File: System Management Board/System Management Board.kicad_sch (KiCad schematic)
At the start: 21 parts

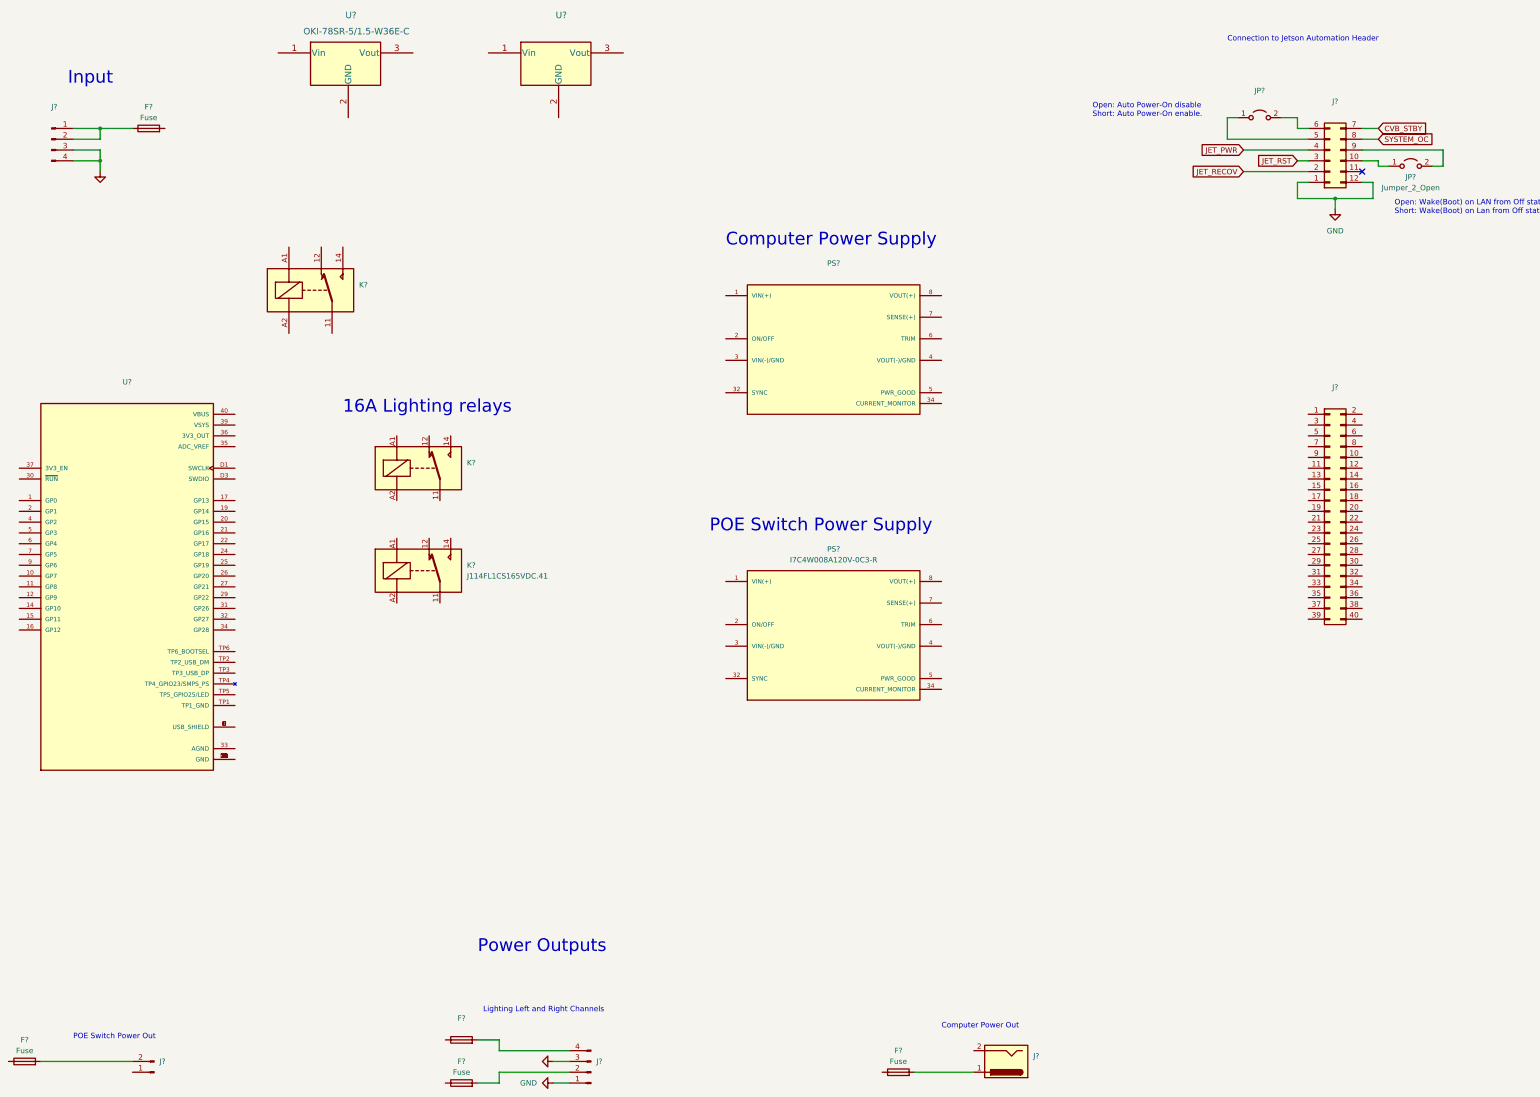
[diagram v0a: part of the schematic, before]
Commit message: Started playing around with layout and mounting of SMB in Enclosure
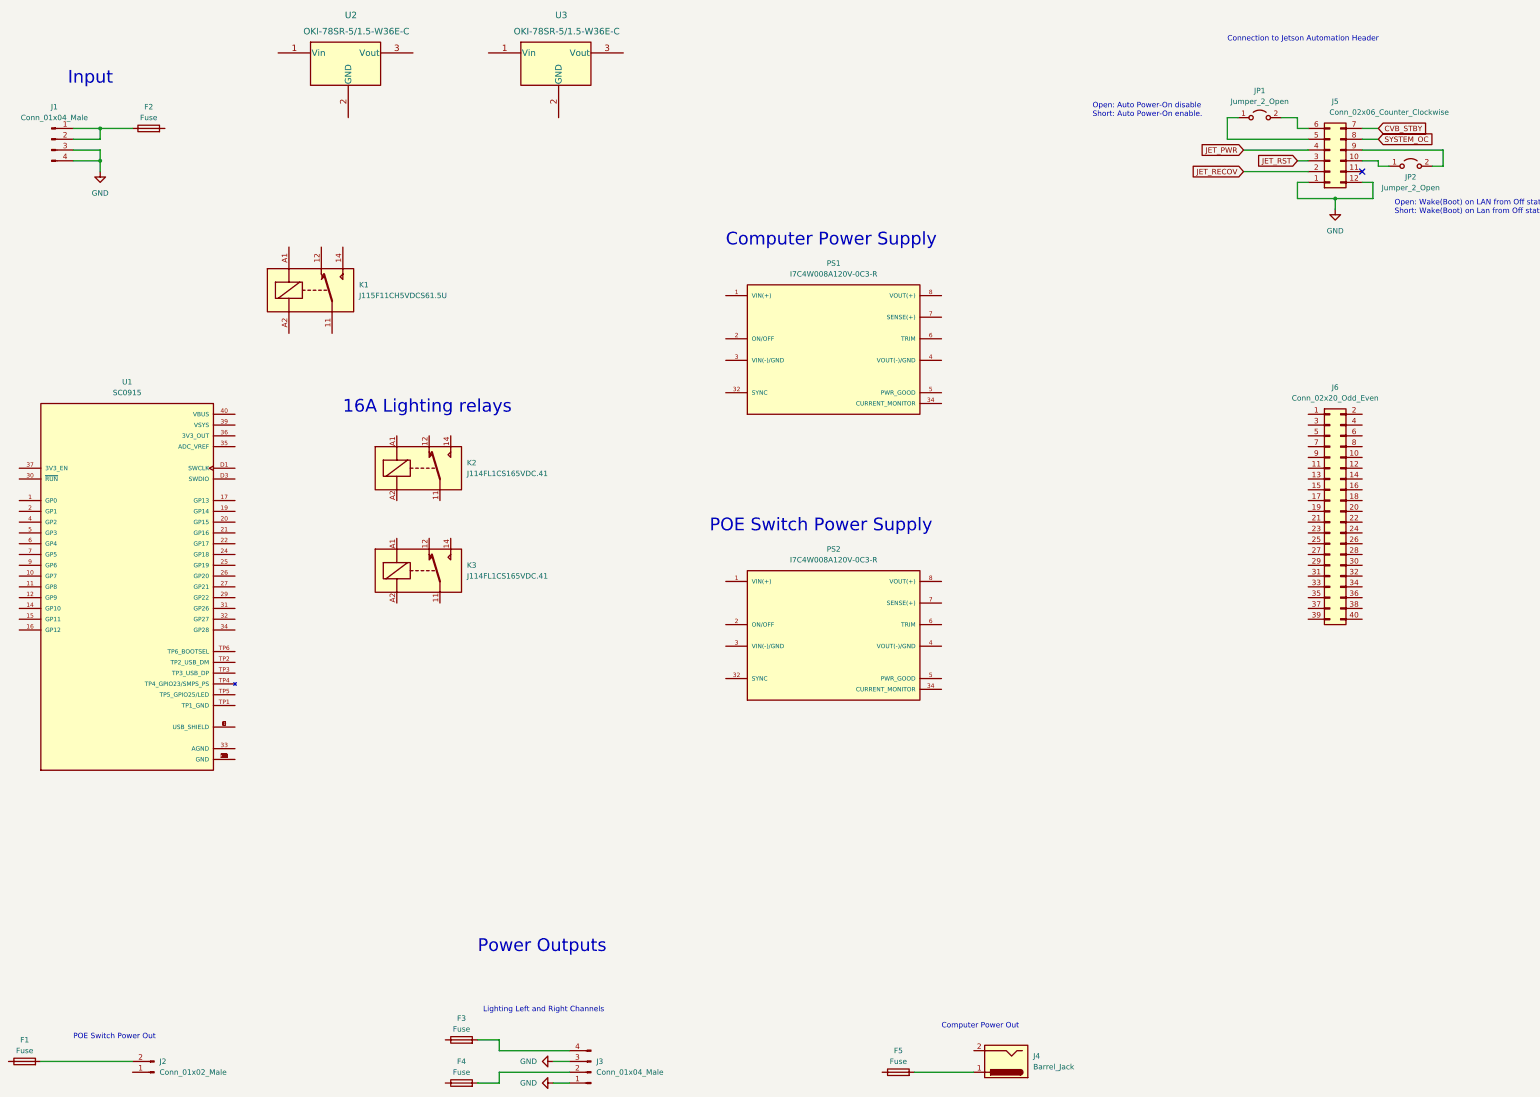
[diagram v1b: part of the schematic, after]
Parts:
- F3: renamed from F?; value (none) -> Fuse
- J1, J3: renamed from J?; value (none) -> Conn_01x04_Male
- J2: renamed from J?; value (none) -> Conn_01x02_Male
- J4: renamed from J?; value (none) -> Barrel_Jack
- J5: renamed from J?; value (none) -> Conn_02x06_Counter_Clockwise
- J6: renamed from J?; value (none) -> Conn_02x20_Odd_Even; footprint (none) -> Connector_PinSocket_2.54mm:PinSocket_2x20_P2.54mm_Horizontal
- JP1: renamed from JP?; value (none) -> Jumper_2_Open
- K1: renamed from K?; value (none) -> J115F11CH5VDCS61.5U; footprint (none) -> SMB:Relay_SPDT_RAYEX-L90S
- K2: renamed from K?; value (none) -> J114FL1CS165VDC.41; footprint (none) -> SMB:Relay_SPDT_Schrack-RT1-16A-FormC_RM5mm
- PS1: renamed from PS?; value (none) -> I7C4W008A120V-0C3-R; footprint (none) -> SMB:CONV_I7C4W008A120V-0C3-R
- PS2: renamed from PS?; footprint CONV_I7C4W008A120V-0C3-R -> SMB:CONV_I7C4W008A120V-0C3-R
- U1: renamed from U?; value (none) -> SC0915; footprint (none) -> SMB:MODULE_SC0915
- U3: renamed from U?; value (none) -> OKI-78SR-5/1.5-W36E-C
- gave numbers to parts that had none: 7

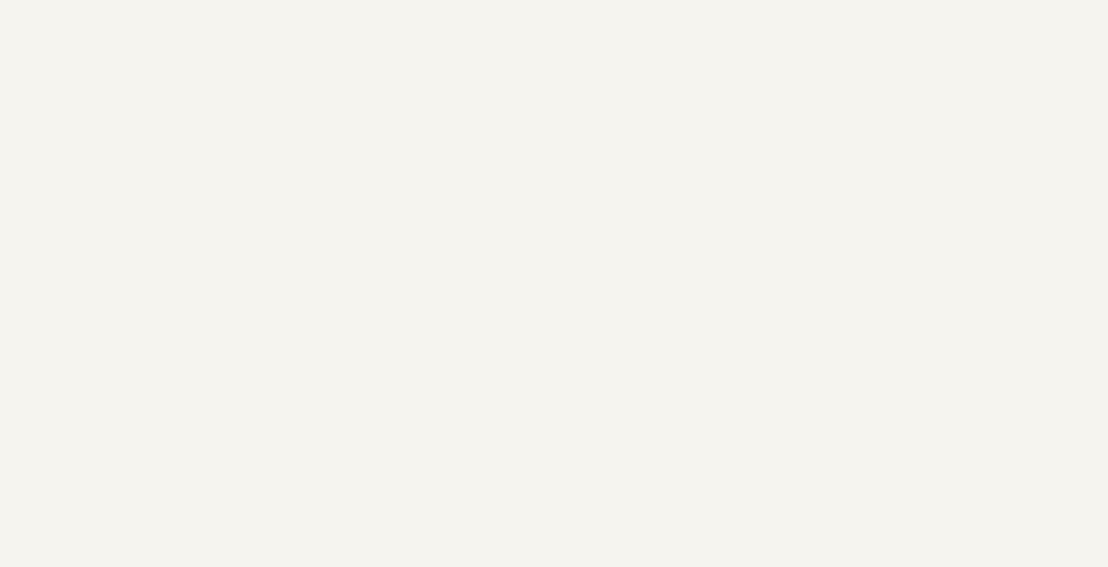
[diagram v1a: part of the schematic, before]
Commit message: Fixed solidworks brainmelt from last commit and moved PCb template into Kicad
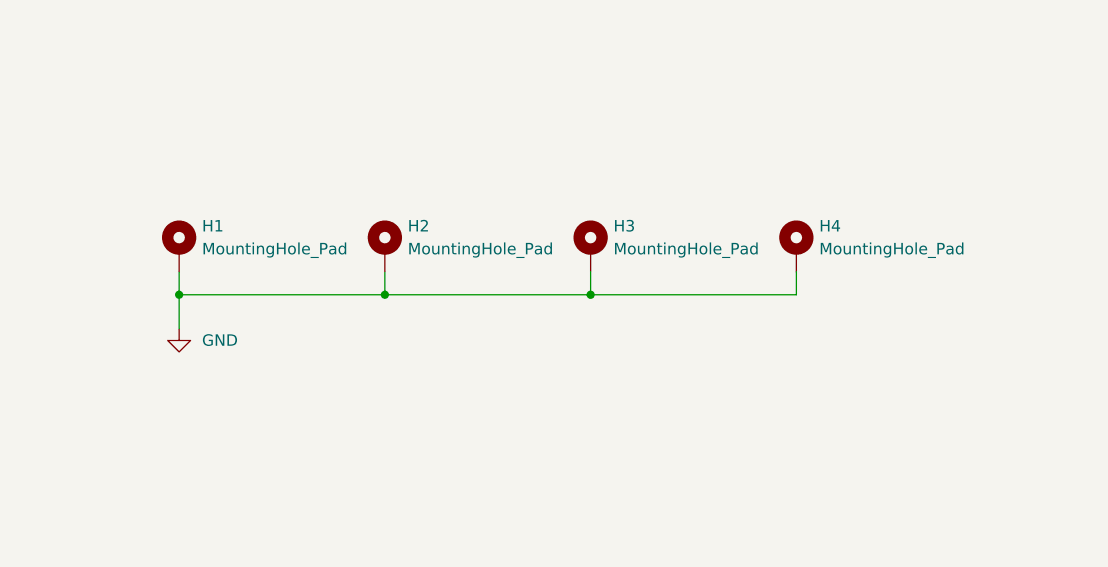
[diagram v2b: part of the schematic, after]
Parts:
- added H1, H2, H3, H4: MountingHole_Pad, MountingHole:MountingHole_3.2mm_M3_DIN965_Pad, symbol Mechanical:MountingHole_Pad
- J6: footprint Connector_PinSocket_2.54mm:PinSocket_2x20_P2.54mm_Horizontal -> Connector_PinHeader_2.54mm:PinHeader_2x20_P2.54mm_Horizontal
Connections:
- net GND: now also H1.1, H2.1, H3.1, H4.1
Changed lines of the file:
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@@
   (junction (at 48.26 45.72) (diameter 0) (color 0 0 0 0)
+  )
+  (junction (at 359.41 240.03) (diameter 0) (color 0 0 0 0)
+  )
+  (junction (at 336.55 240.03) (diameter 0) (color 0 0 0 0)
+  )
+  (junction (at 313.69 240.03) (diameter 0) (color 0 0 0 0)
   )
   (junction (at 339.09 62.23) (diameter 0) (color 0 0 0 0)
@@
     (stroke (width 0) (type default) (color 0 0 0 0))
   )
+  (wire (pts (xy 336.55 240.03) (xy 359.41 240.03))
+    (stroke (width 0) (type default) (color 0 0 0 0))
+  )
+  (wire (pts (xy 359.41 240.03) (xy 382.27 240.03))
+    (stroke (width 0) (type default) (color 0 0 0 0))
+  )
+  (wire (pts (xy 382.27 237.49) (xy 382.27 240.03))
+    (stroke (width 0) (type default) (color 0 0 0 0))
+  )
   (wire (pts (xy 351.79 54.61) (xy 349.25 54.61))
     (stroke (width 0) (type default) (color 0 0 0 0))
@@
     (stroke (width 0) (type default) (color 0 0 0 0))
   )
+  (wire (pts (xy 313.69 240.03) (xy 313.69 243.84))
+    (stroke (width 0) (type default) (color 0 0 0 0))
+  )
   (wire (pts (xy 317.5 50.8) (xy 332.74 50.8))
     (stroke (width 0) (type default) (color 0 0 0 0))
@@
     (stroke (width 0) (type default) (color 0 0 0 0))
   )
+  (wire (pts (xy 359.41 237.49) (xy 359.41 240.03))
+    (stroke (width 0) (type default) (color 0 0 0 0))
+  )
+  (wire (pts (xy 313.69 240.03) (xy 336.55 240.03))
+    (stroke (width 0) (type default) (color 0 0 0 0))
+  )
   (wire (pts (xy 364.49 50.8) (xy 364.49 54.61))
     (stroke (width 0) (type default) (color 0 0 0 0))
@@
     (stroke (width 0) (type default) (color 0 0 0 0))
   )
+  (wire (pts (xy 313.69 237.49) (xy 313.69 240.03))
+    (stroke (width 0) (type default) (color 0 0 0 0))
+  )
   (wire (pts (xy 330.2 62.23) (xy 339.09 62.23))
+    (stroke (width 0) (type default) (color 0 0 0 0))
+  )
+  (wire (pts (xy 336.55 237.49) (xy 336.55 240.03))
     (stroke (width 0) (type default) (color 0 0 0 0))
   )
@@
     (pin "2")
   )
+  (symbol (lib_id "Mechanical:MountingHole_Pad") (at 313.69 234.95 0) (unit 1)
+    (in_bom yes) (on_board yes) (fields_autoplaced)
+    (property "Reference" "H1" (id 0) (at 316.23 232.4099 0)
+      (effects (font (size 1.27 1.27)) (justify left))
+    )
+    (property "Value" "MountingHole_Pad" (id 1) (at 316.23 234.9499 0)
+      (effects (font (size 1.27 1.27)) (justify left))
+    )
+    (property "Footprint" "MountingHole:MountingHole_3.2mm_M3_DIN965_Pad" (id 2) (at 313.69 234.95 0)
+      (effects (font (size 1.27 1.27)) hide)
+    )
+    (property "Datasheet" "~" (id 3) (at 313.69 234.95 0)
+      (effects (font (size 1.27 1.27)) hide)
+    )
+    (pin "1")
+  )
   (symbol (lib_id "Jumper:Jumper_2_Open") (at 356.87 54.61 0) (unit 1)
     (in_bom yes) (on_board yes)
@@
     (pin "1")
     (pin "2")
+  )
+  (symbol (lib_id "Mechanical:MountingHole_Pad") (at 382.27 234.95 0) (unit 1)
+    (in_bom yes) (on_board yes) (fields_autoplaced)
+    (property "Reference" "H4" (id 0) (at 384.81 232.4099 0)
+      (effects (font (size 1.27 1.27)) (justify left))
+    )
+    (property "Value" "MountingHole_Pad" (id 1) (at 384.81 234.9499 0)
+      (effects (font (size 1.27 1.27)) (justify left))
+    )
+    (property "Footprint" "MountingHole:MountingHole_3.2mm_M3_DIN965_Pad" (id 2) (at 382.27 234.95 0)
+      (effects (font (size 1.27 1.27)) hide)
+    )
+    (property "Datasheet" "~" (id 3) (at 382.27 234.95 0)
+      (effects (font (size 1.27 1.27)) hide)
+    )
+    (pin "1")
   )
   (symbol (lib_id "Device:Fuse") (at 133.35 270.51 90) (unit 1)
@@
     (property "Reference" "J6" (id 0) (at 339.09 106.68 0))
     (property "Value" "Conn_02x20_Odd_Even" (id 1) (at 339.09 109.22 0))
-    (property "Footprint" "Connector_PinSocket_2.54mm:PinSocket_2x20_P2.54mm_Horizontal" (id 2) (at 337.82 135.89 0)
+    (property "Footprint" "Connector_PinHeader_2.54mm:PinHeader_2x20_P2.54mm_Horizontal" (id 2) (at 337.82 135.89 0)
       (effects (font (size 1.27 1.27)) hide)
     )
@@
     (pin "9")
   )
+  (symbol (lib_id "power:GND") (at 313.69 243.84 0) (unit 1)
+    (in_bom yes) (on_board yes) (fields_autoplaced)
+    (property "Reference" "#PWR0105" (id 0) (at 313.69 250.19 0)
+      (effects (font (size 1.27 1.27)) hide)
+    )
+    (property "Value" "GND" (id 1) (at 316.23 245.1099 0)
+      (effects (font (size 1.27 1.27)) (justify left))
+    )
+    (property "Footprint" "" (id 2) (at 313.69 243.84 0)
+      (effects (font (size 1.27 1.27)) hide)
+    )
+    (property "Datasheet" "" (id 3) (at 313.69 243.84 0)
+      (effects (font (size 1.27 1.27)) hide)
+    )
+    (pin "1")
+  )
   (symbol (lib_id "Device:Fuse") (at 59.69 45.72 90) (unit 1)
     (in_bom yes) (on_board yes)
@@
     (pin "1")
   )
+  (symbol (lib_id "Mechanical:MountingHole_Pad") (at 336.55 234.95 0) (unit 1)
+    (in_bom yes) (on_board yes) (fields_autoplaced)
+    (property "Reference" "H2" (id 0) (at 339.09 232.4099 0)
+      (effects (font (size 1.27 1.27)) (justify left))
+    )
+    (property "Value" "MountingHole_Pad" (id 1) (at 339.09 234.9499 0)
+      (effects (font (size 1.27 1.27)) (justify left))
+    )
+    (property "Footprint" "MountingHole:MountingHole_3.2mm_M3_DIN965_Pad" (id 2) (at 336.55 234.95 0)
+      (effects (font (size 1.27 1.27)) hide)
+    )
+    (property "Datasheet" "~" (id 3) (at 336.55 234.95 0)
+      (effects (font (size 1.27 1.27)) hide)
+    )
+    (pin "1")
+  )
   (symbol (lib_id "SMB:OKI-78SR-5{brace}slash}1.5-W36E-C") (at 107.95 27.94 0) (unit 1)
     (in_bom yes) (on_board yes)
@@
     (pin "2")
     (pin "3")
+  )
+  (symbol (lib_id "Mechanical:MountingHole_Pad") (at 359.41 234.95 0) (unit 1)
+    (in_bom yes) (on_board yes) (fields_autoplaced)
+    (property "Reference" "H3" (id 0) (at 361.95 232.4099 0)
+      (effects (font (size 1.27 1.27)) (justify left))
+    )
+    (property "Value" "MountingHole_Pad" (id 1) (at 361.95 234.9499 0)
+      (effects (font (size 1.27 1.27)) (justify left))
+    )
+    (property "Footprint" "MountingHole:MountingHole_3.2mm_M3_DIN965_Pad" (id 2) (at 359.41 234.95 0)
+      (effects (font (size 1.27 1.27)) hide)
+    )
+    (property "Datasheet" "~" (id 3) (at 359.41 234.95 0)
+      (effects (font (size 1.27 1.27)) hide)
+    )
+    (pin "1")
   )
   (symbol (lib_id "Connector:Barrel_Jack") (at 261.62 265.43 180) (unit 1)
@@
       (reference "#PWR0104") (unit 1) (value "GND") (footprint "")
     )
+    (path "/73bba062-1b3e-4448-92cb-25c1fd00c4c6"
+      (reference "#PWR0105") (unit 1) (value "GND") (footprint "")
+    )
     (path "/c2cb5849-1a7a-473c-8a0e-9d2b76698dc0"
       (reference "F1") (unit 1) (value "Fuse") (footprint "")
@@
       (reference "F5") (unit 1) (value "Fuse") (footprint "")
     )
+    (path "/31fbff98-a40a-4148-9e31-9912fa3bb769"
+      (reference "H1") (unit 1) (value "MountingHole_Pad") (footprint "MountingHole:MountingHole_3.2mm_M3_DIN965_Pad")
+    )
+    (path "/985c27ee-fc67-4c32-a67f-6e24dbf21a3d"
+      (reference "H2") (unit 1) (value "MountingHole_Pad") (footprint "MountingHole:MountingHole_3.2mm_M3_DIN965_Pad")
+    )
+    (path "/b403c61c-29f8-4281-a486-db5cc50a75f2"
+      (reference "H3") (unit 1) (value "MountingHole_Pad") (footprint "MountingHole:MountingHole_3.2mm_M3_DIN965_Pad")
+    )
+    (path "/3df9b30d-7128-4372-b4bf-908783760212"
+      (reference "H4") (unit 1) (value "MountingHole_Pad") (footprint "MountingHole:MountingHole_3.2mm_M3_DIN965_Pad")
+    )
     (path "/a63b7d18-8561-4d9b-b766-d84503873d1f"
       (reference "J1") (unit 1) (value "Conn_01x04_Male") (footprint "")
@@
     )
     (path "/6f34aafb-fa97-4ad5-b6b3-1fba80dd5d47"
-      (reference "J6") (unit 1) (value "Conn_02x20_Odd_Even") (footprint "Connector_PinSocket_2.54mm:PinSocket_2x20_P2.54mm_Horizontal")
+      (reference "J6") (unit 1) (value "Conn_02x20_Odd_Even") (footprint "Connector_PinHeader_2.54mm:PinHeader_2x20_P2.54mm_Horizontal")
     )
     (path "/d7b7465f-9856-4f51-bc13-45843f087272"
